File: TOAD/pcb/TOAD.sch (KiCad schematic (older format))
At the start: 151 parts, among them IC1 STM32F405RxTx, IC10 ADP3335, IC11 CS2100-CP, IC12 BGS12AL7, IC13 SL18860DC, IC2 Si4463, IC3 MAX-M8Q, IC4 SN74LVC1G0832, IC5 BGS12AL7, IC6 ADP3335, IC7 BQ24232HA, IC8 NC7SZ04, IC9 Si4463, J1 USB, J2 BATT, J3 SWITCH, P1 SMA, P2 SWD_TC, P3 SMA, P4 SMA, U1 MICROSD, X1 USB Cap, X10 RF Frame, X11 RF Cover, X12 Mount, X13 Mount, X14 RF Frame, X15 RF Cover, X2 USB Mini-B, X3 Case, X4 SMA Panel, X5 SMA Panel, X6 PWR Switch, X7 Battery, X8 Mount, X9 Mount, Y1 26M TCXO

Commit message: folder organisation and BOM
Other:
- note added: "See ../documentation/RangingSpecs.pdf for further notes"
- note removed: "See /RangingSpecs.pdf for further notes"
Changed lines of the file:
@@
 	0    -1   -1   0
 $EndComp
-Text Notes 14100 10750 0    60   ~ 0
-See /RangingSpecs.pdf for further notes
+Text Notes 13300 10750 0    60   ~ 0
+See ../documentation/RangingSpecs.pdf for further notes
 $Comp
 L C_Small C26

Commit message: pcb complete
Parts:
- added TP1, TP10, TP11, TP12, TP2, TP3, TP4, TP5, TP6, TP7, TP8, TP9: TESTPAD, agg:TESTPAD, symbol TESTPAD
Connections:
- net GPS_PPS: now also TP1.1 (TP)
- net I2C1_SCL: now also TP8.1 (TP)
- net I2C1_SDA: now also TP7.1 (TP)
- net PR_GPIO: now also TP12.1 (TP)
- net SPI1_MISO: now also TP5.1 (TP)
- net SPI1_MOSI: now also TP6.1 (TP)
- net SPI1_SCK: now also TP4.1 (TP)
- net SPI2_MISO: now also TP10.1 (TP)
- net SPI2_MOSI: now also TP11.1 (TP)
- net SPI2_SCK: now also TP9.1 (TP)
- net USART1_RX: now also TP3.1 (TP)
- net USART1_TX: now also TP2.1 (TP)
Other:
- note removed: "TODO:\n- Via Stitching\n- Test Points\n- Silkscreen & Logos\n- Gerbers\n- BOM\n- Boardholder STL"

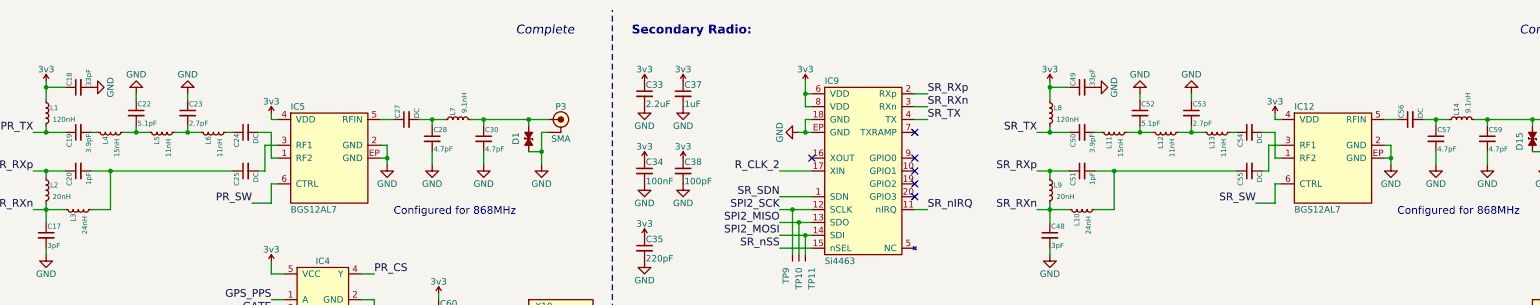
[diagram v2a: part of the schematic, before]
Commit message: removed DC blocking caps from radios
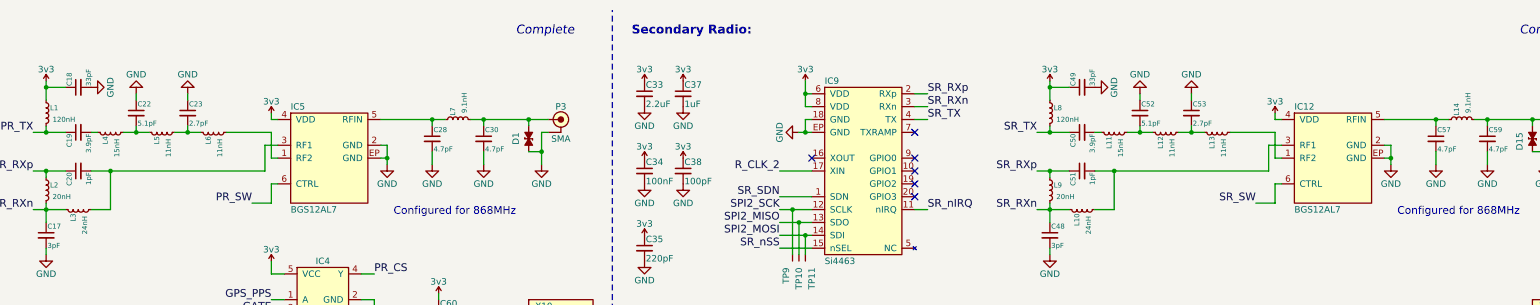
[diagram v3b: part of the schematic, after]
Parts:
- removed C24, C25, C27, C54, C55, C56: DC, agg:0402, symbol C_Small
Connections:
- net at C20.2, L3.2: now also IC5.3 (RF1)
- net at IC5.1 (RF2): now also L6.2
- net at IC5.5 (RFIN): now also C28.1, L7.1
- net at C51.2, L10.2: now also IC12.3 (RF1)
- net at IC12.1 (RF2): now also L13.2
- net at IC12.5 (RFIN): now also C57.1, L14.1
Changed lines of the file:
@@
-$EndComp
-$Comp
-L C_Small C27
-U 1 1 58EBA3B1
-P 6700 1350
-F 0 "C27" H 6710 1420 39  0000 L CNN
-F 1 "DC" H 6710 1270 39  0000 L CNN
-F 2 "agg:0402" H 6700 1350 50  0001 C CNN
-F 3 "" H 6700 1350 50  0001 C CNN
-	1    6700 1350
-	0    -1   -1   0
-$EndComp
-$Comp
-L C_Small C24
-U 1 1 58EBBE01
-P 5450 1450
-F 0 "C24" H 5460 1520 39  0000 L CNN
-F 1 "DC" H 5460 1370 39  0000 L CNN
-F 2 "agg:0402" H 5450 1450 50  0001 C CNN
-F 3 "" H 5450 1450 50  0001 C CNN
-	1    5450 1450
-	0    -1   1    0
-$EndComp
-$Comp
-L C_Small C25
-U 1 1 58EBD9E7
-P 5450 1750
-F 0 "C25" H 5460 1820 39  0000 L CNN
-F 1 "DC" H 5460 1670 39  0000 L CNN
-F 2 "agg:0402" H 5450 1750 50  0001 C CNN
-F 3 "" H 5450 1750 50  0001 C CNN
-	1    5450 1750
-	0    -1   1    0
 $EndComp
 $Comp
@@
 $EndComp
 $Comp
-L C_Small C56
-U 1 1 58ECABFF
-P 14500 1350
-F 0 "C56" H 14510 1420 39  0000 L CNN
-F 1 "DC" H 14510 1270 39  0000 L CNN
-F 2 "agg:0402" H 14500 1350 50  0001 C CNN
-F 3 "" H 14500 1350 50  0001 C CNN
-	1    14500 1350
-	0    -1   -1   0
-$EndComp
-$Comp
-L C_Small C54
-U 1 1 58ECAC09
-P 13250 1450
-F 0 "C54" H 13260 1520 39  0000 L CNN
-F 1 "DC" H 13260 1370 39  0000 L CNN
-F 2 "agg:0402" H 13250 1450 50  0001 C CNN
-F 3 "" H 13250 1450 50  0001 C CNN
-	1    13250 1450
-	0    -1   1    0
-$EndComp
-$Comp
-L C_Small C55
-U 1 1 58ECAC15
-P 13250 1750
-F 0 "C55" H 13260 1820 39  0000 L CNN
-F 1 "DC" H 13260 1670 39  0000 L CNN
-F 2 "agg:0402" H 13250 1750 50  0001 C CNN
-F 3 "" H 13250 1750 50  0001 C CNN
-	1    13250 1750
-	0    -1   1    0
-$EndComp
-$Comp
 L L_Small L13
 U 1 1 58ECAC22
@@
 	11050 4050 11750 4050
 Wire Wire Line
-	6600 1350 6500 1350
-Wire Wire Line
-	6800 1350 7000 1350
+	6500 1350 7000 1350
 Wire Wire Line
 	6900 1350 6900 1400
 Connection ~ 6900 1350
 Wire Wire Line
-	4250 1750 5350 1750
+	4250 1750 5600 1750
 Connection ~ 4400 1750
 Wire Wire Line
-	5300 1450 5350 1450
+	5300 1450 5650 1450
 Wire Wire Line
 	5500 2000 5650 2000
@@
 	11700 2350 11700 2400
 Wire Wire Line
-	14400 1350 14300 1350
-Wire Wire Line
-	14600 1350 14800 1350
+	14300 1350 14800 1350
 Wire Wire Line
 	14700 1350 14700 1400
 Connection ~ 14700 1350
 Wire Wire Line
-	12050 1750 13150 1750
+	12050 1750 13400 1750
 Connection ~ 12200 1750
 Wire Wire Line
-	13100 1450 13150 1450
+	13100 1450 13450 1450
 Wire Wire Line
 	13300 2000 13450 2000
@@
 	13450 1850 13500 1850
 Wire Wire Line
-	5550 1750 5600 1750
-Wire Wire Line
 	5600 1750 5600 1550
 Wire Wire Line
 	5600 1550 5700 1550
 Wire Wire Line
-	5550 1450 5650 1450
-Wire Wire Line
 	5650 1450 5650 1650
 Wire Wire Line
 	5650 1650 5700 1650
 Wire Wire Line
-	13350 1750 13400 1750
-Wire Wire Line
 	13400 1750 13400 1550
 Wire Wire Line
 	13400 1550 13500 1550
 Wire Wire Line
-	13350 1450 13450 1450
-Wire Wire Line
 	13450 1450 13450 1650

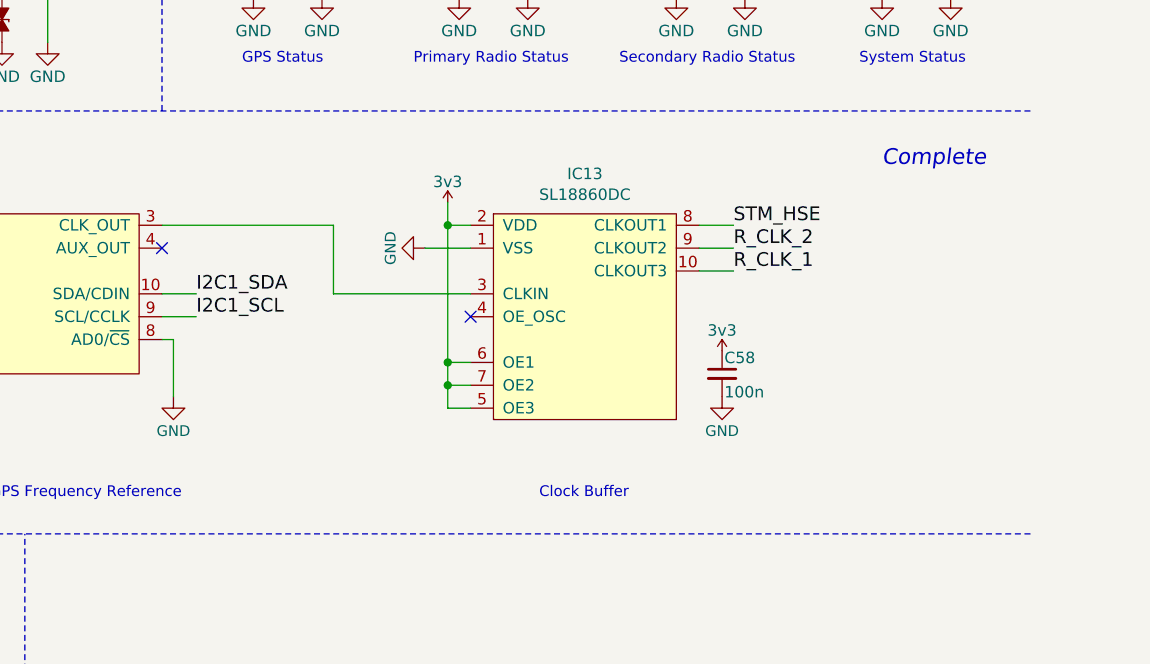
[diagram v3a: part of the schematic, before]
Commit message: added radio clock dividers
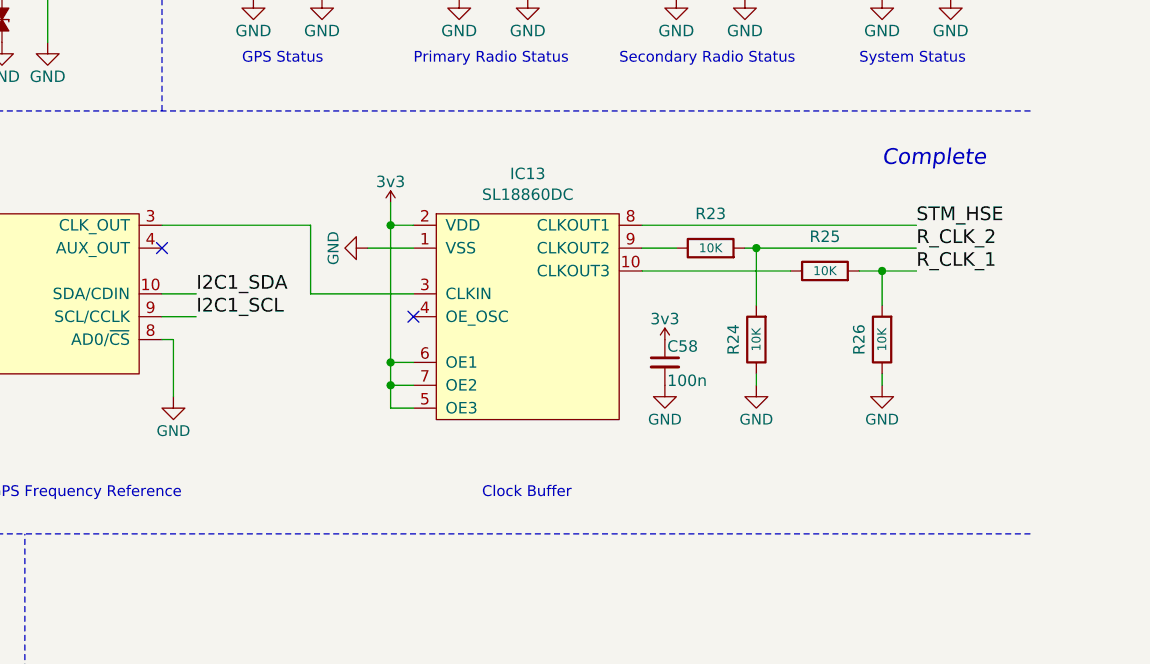
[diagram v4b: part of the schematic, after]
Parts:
- added R23, R24, R25, R26: 10K, agg:0402, symbol R-RESCUE-TOAD
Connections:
- net GND: now also R24.1, R26.1
- net R_CLK_1: now also R25.2, R26.2; no longer IC13.10 (CLKOUT3)
- net R_CLK_2: now also R23.2, R24.2; no longer IC13.9 (CLKOUT2)
- new net: IC13.10 (CLKOUT3), R25.1
- new net: IC13.9 (CLKOUT2), R23.1
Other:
- moved on the sheet: C58, IC13
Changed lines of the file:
@@
 $EndComp
 $Comp
-L GND-RESCUE-TOAD #PWR142
+L GND-RESCUE-TOAD #PWR144
 U 1 1 5872B793
 P 15700 4850
-F 0 "#PWR142" H 15700 4600 50  0001 C CNN
+F 0 "#PWR144" H 15700 4600 50  0001 C CNN
 F 1 "GND" H 15700 4700 50  0000 C CNN
 F 2 "" H 15700 4850 50  0000 C CNN
@@
 $EndComp
 $Comp
-L GND-RESCUE-TOAD #PWR140
+L GND-RESCUE-TOAD #PWR141
 U 1 1 5872B7A9
 P 15400 4850
-F 0 "#PWR140" H 15400 4600 50  0001 C CNN
+F 0 "#PWR141" H 15400 4600 50  0001 C CNN
 F 1 "GND" H 15400 4700 50  0000 C CNN
 F 2 "" H 15400 4850 50  0000 C CNN
@@
 F 1 "CS2100-CP" H 10950 5750 50  0000 L CNN
 F 2 "agg:MSOP-10" H 10950 5650 50  0001 L CNN
-F 3 "https://www.cirrus.com/en/pubs/proDatasheet/CS2100-CP_F3.pdf" H 10950 5550 50  0001 L CNN
+F 3 "http://www.farnell.com/datasheets/51788.pdf" H 10950 5550 50  0001 L CNN
 F 4 "777-CS2100CP-CZZ" H 10950 5450 50  0001 L CNN "Mouser"
 	1    11550 6150
@@
 $EndComp
 $Comp
-L GND-RESCUE-TOAD #PWR134
+L GND-RESCUE-TOAD #PWR136
 U 1 1 58868A40
 P 14500 4850
-F 0 "#PWR134" H 14500 4600 50  0001 C CNN
+F 0 "#PWR136" H 14500 4600 50  0001 C CNN
 F 1 "GND" H 14500 4700 50  0000 C CNN
 F 2 "" H 14500 4850 50  0000 C CNN
@@
 L SL18860DC IC13
 U 1 1 58BF1CB3
-P 14100 6250
-F 0 "IC13" H 14100 6875 50  0000 C CNN
-F 1 "SL18860DC" H 14100 6784 50  0000 C CNN
-F 2 "agg:DFN-10-SL18860DC" H 50  -1750 50  0001 L CNN
-F 3 "http://www.silabs.com/Support%20Documents/TechnicalDocs/SL18860.pdf" H 50  -1850 50  0001 L CNN
-F 4 "634-SL18860DC" H 50  -1950 50  0001 L CNN "Mouser"
-	1    14100 6250
+P 13850 6250
+F 0 "IC13" H 13850 6875 50  0000 C CNN
+F 1 "SL18860DC" H 13850 6784 50  0000 C CNN
+F 2 "agg:DFN-10-SL18860DC" H -200 -1750 50  0001 L CNN
+F 3 "http://www.silabs.com/Support%20Documents/TechnicalDocs/SL18860.pdf" H -200 -1850 50  0001 L CNN
+F 4 "634-SL18860DC" H -200 -1950 50  0001 L CNN "Mouser"
+	1    13850 6250
 	1    0    0    -1
 $EndComp
-NoConn ~ 13600 6250
+NoConn ~ 13350 6250
 $Comp
 L GND-RESCUE-TOAD #PWR128
 U 1 1 58BFC7C6
-P 13400 5950
-F 0 "#PWR128" H 13400 5700 31  0001 C CNN
-F 1 "GND" H 13400 5800 47  0000 C CNN
-F 2 "" H 13400 5950 50  0000 C CNN
-F 3 "" H 13400 5950 50  0000 C CNN
-	1    13400 5950
+P 13150 5950
+F 0 "#PWR128" H 13150 5700 31  0001 C CNN
+F 1 "GND" H 13150 5800 47  0000 C CNN
+F 2 "" H 13150 5950 50  0000 C CNN
+F 3 "" H 13150 5950 50  0000 C CNN
+	1    13150 5950
 	0    1    1    0
 $EndComp
 $Comp
-L 3v3 #PWR130
+L 3v3 #PWR129
 U 1 1 58BFDEAC
-P 13500 5750
-F 0 "#PWR130" H 13500 5860 50  0001 L CNN
-F 1 "3v3" H 13500 5840 50  0000 C CNN
-F 2 "" H 13500 5750 60  0000 C CNN
-F 3 "" H 13500 5750 60  0000 C CNN
-	1    13500 5750
+P 13250 5750
+F 0 "#PWR129" H 13250 5860 50  0001 L CNN
+F 1 "3v3" H 13250 5840 50  0000 C CNN
+F 2 "" H 13250 5750 60  0000 C CNN
+F 3 "" H 13250 5750 60  0000 C CNN
+	1    13250 5750
 	1    0    0    -1
 $EndComp
 $Comp
-L GND-RESCUE-TOAD #PWR137
+L GND-RESCUE-TOAD #PWR135
 U 1 1 58C16E59
-P 14700 6600
-F 0 "#PWR137" H 14700 6350 31  0001 C CNN
-F 1 "GND" H 14700 6450 47  0000 C CNN
-F 2 "" H 14700 6600 50  0000 C CNN
-F 3 "" H 14700 6600 50  0000 C CNN
-	1    14700 6600
+P 14450 6550
+F 0 "#PWR135" H 14450 6300 31  0001 C CNN
+F 1 "GND" H 14450 6400 47  0000 C CNN
+F 2 "" H 14450 6550 50  0000 C CNN
+F 3 "" H 14450 6550 50  0000 C CNN
+	1    14450 6550
 	1    0    0    -1
 $EndComp
 $Comp
-L 3v3 #PWR136
+L 3v3 #PWR134
 U 1 1 58C16E5F
-P 14700 6400
-F 0 "#PWR136" H 14700 6510 50  0001 L CNN
-F 1 "3v3" H 14700 6490 50  0000 C CNN
-F 2 "" H 14700 6400 60  0000 C CNN
-F 3 "" H 14700 6400 60  0000 C CNN
-	1    14700 6400
+P 14450 6350
+F 0 "#PWR134" H 14450 6460 50  0001 L CNN
+F 1 "3v3" H 14450 6440 50  0000 C CNN
+F 2 "" H 14450 6350 60  0000 C CNN
+F 3 "" H 14450 6350 60  0000 C CNN
+	1    14450 6350
 	1    0    0    -1
 $EndComp
-Text Notes 13900 7050 0    47   ~ 0
+Text Notes 13650 7050 0    47   ~ 0
 Clock Buffer
-Text Label 14750 5850 0    60   ~ 0
+Text Label 15550 5850 0    60   ~ 0
 STM_HSE
-Text Label 14750 6050 0    60   ~ 0
+Text Label 15550 6050 0    60   ~ 0
 R_CLK_1
-Text Label 14750 5950 0    60   ~ 0
+Text Label 15550 5950 0    60   ~ 0
 R_CLK_2
 Text Label 1750 6400 2    60   ~ 0
@@
 L C_Small C58
 U 1 1 58E0A265
-P 14700 6500
-F 0 "C58" H 14710 6570 50  0000 L CNN
-F 1 "100n" H 14710 6420 50  0000 L CNN
-F 2 "agg:0603-L" H 14700 6500 50  0001 C CNN
-F 3 "" H 14700 6500 50  0000 C CNN
-F 4 "2496834" H 14700 6500 60  0001 C CNN "Farnell"
-	1    14700 6500
+P 14450 6450
+F 0 "C58" H 14460 6520 50  0000 L CNN
+F 1 "100n" H 14460 6370 50  0000 L CNN
+F 2 "agg:0603-L" H 14450 6450 50  0001 C CNN
+F 3 "" H 14450 6450 50  0000 C CNN
+F 4 "2496834" H 14450 6450 60  0001 C CNN "Farnell"
+	1    14450 6450
 	1    0    0    -1
 $EndComp
@@
 $EndComp
 $Comp
-L GND-RESCUE-TOAD #PWR135
+L GND-RESCUE-TOAD #PWR137
 U 1 1 58ECAB14
 P 14700 1700
-F 0 "#PWR135" H 14700 1450 50  0001 C CNN
+F 0 "#PWR137" H 14700 1450 50  0001 C CNN
 F 1 "GND" H 14700 1550 50  0000 C CNN
 F 2 "" H 14700 1700 50  0000 C CNN
@@
 $EndComp
 $Comp
-L GND-RESCUE-TOAD #PWR139
+L GND-RESCUE-TOAD #PWR140
 U 1 1 58ECAB1A
 P 15100 1700
-F 0 "#PWR139" H 15100 1450 50  0001 C CNN
+F 0 "#PWR140" H 15100 1450 50  0001 C CNN
 F 1 "GND" H 15100 1550 50  0000 C CNN
 F 2 "" H 15100 1700 50  0000 C CNN
@@
 $EndComp
 $Comp
-L GND-RESCUE-TOAD #PWR141
+L GND-RESCUE-TOAD #PWR143
 U 1 1 58ECAB40
 P 15550 1700
-F 0 "#PWR141" H 15550 1450 50  0001 C CNN
+F 0 "#PWR143" H 15550 1450 50  0001 C CNN
 F 1 "GND" H 15550 1550 50  0000 C CNN
 F 2 "" H 15550 1700 50  0000 C CNN
@@
 $EndComp
 $Comp
-L 3v3 #PWR129
+L 3v3 #PWR130
 U 1 1 58ECAB72
 P 13450 1300
-F 0 "#PWR129" H 13450 1410 50  0001 L CNN
+F 0 "#PWR130" H 13450 1410 50  0001 L CNN
 F 1 "3v3" H 13450 1390 50  0000 C CNN
 F 2 "" H 13450 1300 60  0000 C CNN
@@
 Connection ~ 9850 7900
 Wire Wire Line
-	12250 5850 13000 5850
-Wire Wire Line
-	13000 5850 13000 6150
-Wire Wire Line
-	13000 6150 13600 6150
-Wire Wire Line
-	13600 5850 13500 5850
+	13350 5850 13250 5850
 Wire Wire Line
-	13500 5750 13500 6650
+	13250 5750 13250 6650
 Wire Wire Line
 	10400 6250 10750 6250
 Wire Wire Line
-	13500 6450 13600 6450
+	13250 6450 13350 6450
 Wire Wire Line
-	13500 6650 13600 6650
+	13250 6650 13350 6650
 Wire Wire Line
-	13600 6550 13500 6550
-Connection ~ 13500 6550
-Connection ~ 13500 6450
+	13350 6550 13250 6550
+Connection ~ 13250 6550
+Connection ~ 13250 6450
 Wire Wire Line
-	14600 5850 14750 5850
+	14350 5850 15550 5850
 Wire Wire Line
-	14600 5950 14750 5950
+	14350 5950 14500 5950
 Wire Wire Line
-	14600 6050 14750 6050
-Connection ~ 13500 5850
+	14350 6050 15000 6050
+Connection ~ 13250 5850
 Wire Wire Line
-	13600 5950 13400 5950
+	13350 5950 13150 5950
 Wire Notes Line
 	5650 7200 16050 7200
@@
 	2900 1700 2900 1650
 Connection ~ 2900 1650
+$Comp
+L R-RESCUE-TOAD R23
+U 1 1 59572180
+P 14650 5950
+F 0 "R23" V 14800 5950 50  0000 C CNN
+F 1 "10K" V 14650 5950 39  0000 C CNN
+F 2 "agg:0402" V 14580 5950 50  0001 C CNN
+F 3 "" H 14650 5950 50  0000 C CNN
+F 4 "2379805" V 14650 5950 60  0001 C CNN "Farnell"
+	1    14650 5950
+	0    -1   -1   0
+$EndComp
+Wire Wire Line
+	12250 5850 12900 5850
+Wire Wire Line
+	12900 5850 12900 6150
+Wire Wire Line
+	12900 6150 13350 6150
+Wire Wire Line
+	14800 5950 15550 5950
+Wire Wire Line
+	15300 6050 15550 6050
+Wire Wire Line
+	14850 6200 14850 5950
+Connection ~ 14850 5950
+Wire Wire Line
+	15400 6050 15400 6200
+Connection ~ 15400 6050
+$Comp
+L GND-RESCUE-TOAD #PWR139
+U 1 1 59579694
+P 14850 6550
+F 0 "#PWR139" H 14850 6300 31  0001 C CNN
+F 1 "GND" H 14850 6400 47  0000 C CNN
+F 2 "" H 14850 6550 50  0000 C CNN
+F 3 "" H 14850 6550 50  0000 C CNN
+	1    14850 6550
+	1    0    0    -1
+$EndComp
+$Comp
+L GND-RESCUE-TOAD #PWR142
+U 1 1 595797E1
+P 15400 6550
+F 0 "#PWR142" H 15400 6300 31  0001 C CNN
+F 1 "GND" H 15400 6400 47  0000 C CNN
+F 2 "" H 15400 6550 50  0000 C CNN
+F 3 "" H 15400 6550 50  0000 C CNN
+	1    15400 6550
+	1    0    0    -1
+$EndComp
+Wire Wire Line
+	15400 6500 15400 6550
+Wire Wire Line
+	14850 6500 14850 6550
+$Comp
+L R-RESCUE-TOAD R25
+U 1 1 5957C987
+P 15150 6050
+F 0 "R25" V 15300 6050 50  0000 C CNN
+F 1 "10K" V 15150 6050 39  0000 C CNN
+F 2 "agg:0402" V 15080 6050 50  0001 C CNN
+F 3 "" H 15150 6050 50  0000 C CNN
+F 4 "2379805" V 15150 6050 60  0001 C CNN "Farnell"
+	1    15150 6050
+	0    -1   -1   0
+$EndComp
+$Comp
+L R-RESCUE-TOAD R24
+U 1 1 5957CAEB
+P 14850 6350
+F 0 "R24" V 14950 6350 50  0000 C CNN
+F 1 "10K" V 14850 6350 39  0000 C CNN
+F 2 "agg:0402" V 14780 6350 50  0001 C CNN
+F 3 "" H 14850 6350 50  0000 C CNN
+F 4 "2379805" V 14850 6350 60  0001 C CNN "Farnell"
+	1    14850 6350
+	-1   0    0    1
+$EndComp
+$Comp
+L R-RESCUE-TOAD R26
+U 1 1 5957D691
+P 15400 6350
+F 0 "R26" V 15500 6350 50  0000 C CNN
+F 1 "10K" V 15400 6350 39  0000 C CNN
+F 2 "agg:0402" V 15330 6350 50  0001 C CNN
+F 3 "" H 15400 6350 50  0000 C CNN
+F 4 "2379805" V 15400 6350 60  0001 C CNN "Farnell"
+	1    15400 6350
+	-1   0    0    1
+$EndComp
 $EndSCHEMATC

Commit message: Most changes completed
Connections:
- net PR_SW: now also IC2.20 (GPIO3); no longer IC1.9 (PC1)
- net SR_SW: now also IC9.20 (GPIO3); no longer IC1.8 (PC0)

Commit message: finalised bom
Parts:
- X1: RS 123-6106 -> 252-163
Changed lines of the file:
@@
 F 2 "" H 5800 10150 50  0001 C CNN
 F 3 "" H 5800 10150 50  0001 C CNN
-F 4 "123-6106" H 5800 10150 60  0001 C CNN "RS"
+F 4 "252-163" H 5800 10150 60  0001 C CNN "RS"
 	1    5800 10150
 	1    0    0    -1
